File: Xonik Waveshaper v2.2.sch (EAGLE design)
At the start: 77 parts, among them IC1 TL074JT, IC2 TL074JT, IC3 TL074JT, IC4 TL072JT, IC5 4013T, IC6 LM311T, T1 2n3904

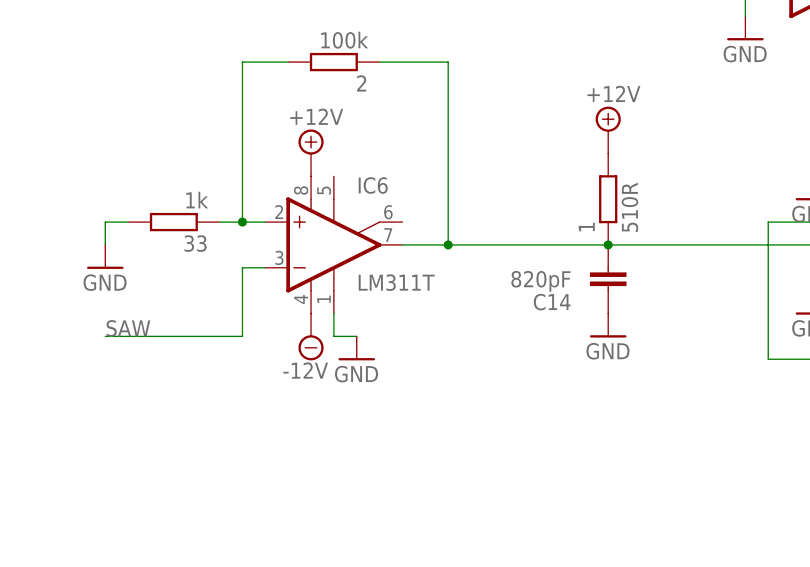
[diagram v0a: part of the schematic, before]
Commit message: Replaced LM311 with SO08 because TSSOP is sold out at JLCPCB
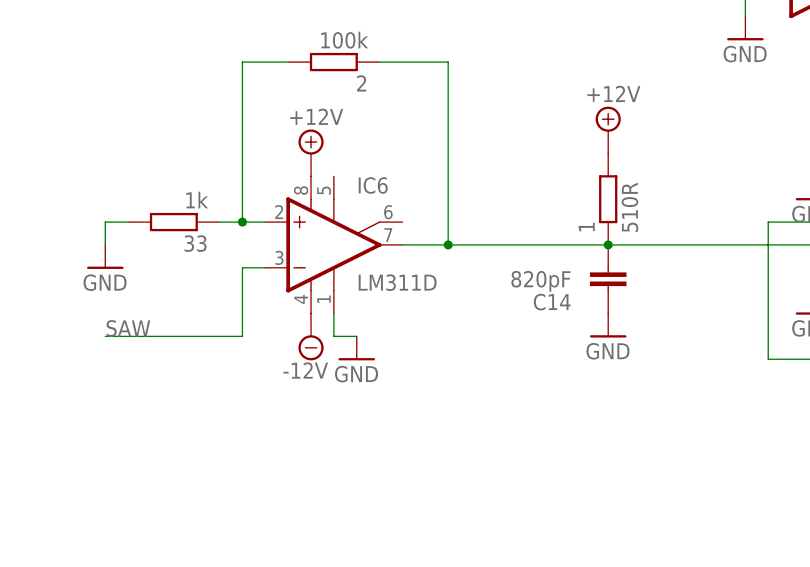
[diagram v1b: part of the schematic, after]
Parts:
- IC6: value LM311T -> LM311D; device joakim:LM311T -> joakim:LM311D
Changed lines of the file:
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@@
 <part name="C12" library="joakim" deviceset="C-EU-J" device="0402" value="1uF"/>
 <part name="C13" library="joakim" deviceset="C-EU-J" device="0402" value="1uF"/>
-<part name="IC6" library="joakim" deviceset="LM311" device="T"/>
+<part name="IC6" library="joakim" deviceset="LM311" device="D" value="LM311D"/>
 <part name="C14" library="joakim" deviceset="C-EU-J" device="0603" value="820pF"/>
 <part name="GND9" library="supply1" library_urn="urn:adsk.eagle:library:371" deviceset="GND" device=""/>

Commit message: Info about trimming
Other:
- note added: "TRIMMING -- To trim the sub oscillators, turn the pw all the way to one side so that it flatlines. The output will now be the sub oscillators only"
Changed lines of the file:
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@@
 <text x="101.6" y="-99.06" size="1.778" layer="97">-5 to 5V</text>
 <text x="101.6" y="-20.32" size="1.778" layer="97">-5 to 5V</text>
+<text x="-177.8" y="63.5" size="3.81" layer="91">TRIMMING
+--
+To trim the sub oscillators, turn the pw all the
+way to one side so that it flatlines. The output
+will now be the sub oscillators only </text>
 </plain>
 <instances>
